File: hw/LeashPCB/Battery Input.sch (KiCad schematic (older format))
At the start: 2 parts, among them J201 1020-1, J202 1020-1

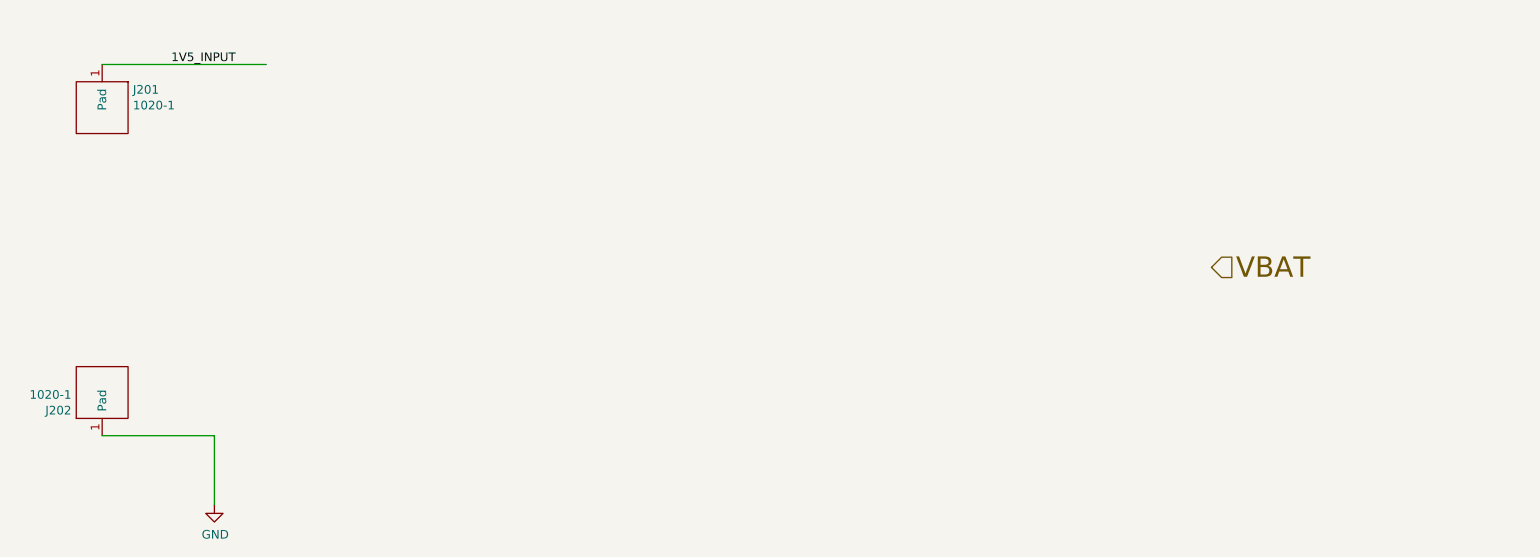
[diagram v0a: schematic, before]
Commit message: Changed some file names to remove spaces and added circuits around the main power chips
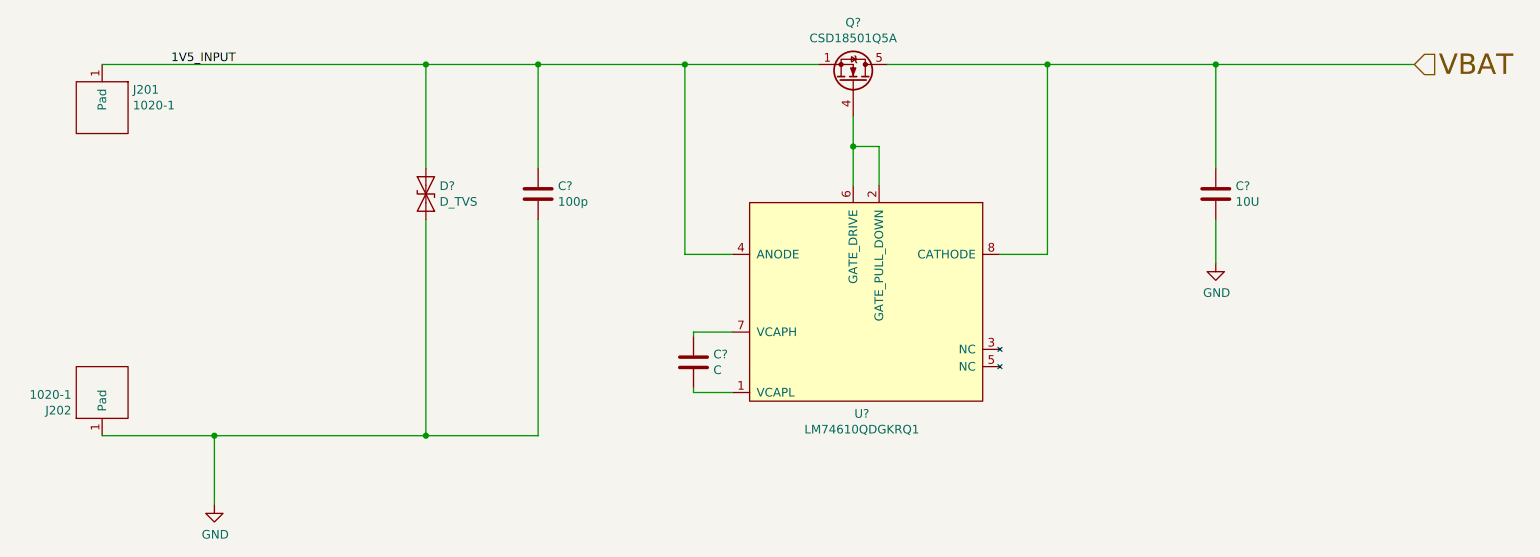
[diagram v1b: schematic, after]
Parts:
- added C?: 100p, symbol Device:C
- added C?: C, symbol Device:C
- added C?: 10U, symbol Device:C
- added D?: D_TVS, symbol Device:D_TVS
- added Q?: CSD18501Q5A, Package_TO_SOT_SMD:TDSON-8-1, symbol Transistor_FET:CSD18501Q5A
- added U?: LM74610QDGKRQ1, symbol LeashPCB:LM74610QDGKRQ1
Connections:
- wire segments 3 -> 29
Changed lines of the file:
@@
 	0    1    1    0
 $EndComp
-Wire Wire Line
-	2650 2050 3600 2050
-Text HLabel 9075 3225 2    118  Input ~ 0
+Text HLabel 10250 2050 2    118  Input ~ 0
 VBAT
 Text Label 3050 2050 0    50   ~ 0
 1V5_INPUT
+$Comp
+L Device:D_TVS D?
+U 1 1 5D067AEF
+P 4525 2800
+F 0 "D?" V 4479 2879 50  0000 L CNN
+F 1 "D_TVS" V 4570 2879 50  0000 L CNN
+F 2 "" H 4525 2800 50  0001 C CNN
+F 3 "~" H 4525 2800 50  0001 C CNN
+	1    4525 2800
+	0    1    1    0
+$EndComp
+$Comp
+L Device:C C?
+U 1 1 5D067F64
+P 5175 2800
+F 0 "C?" H 5290 2846 50  0000 L CNN
+F 1 "100p" H 5290 2755 50  0000 L CNN
+F 2 "" H 5213 2650 50  0001 C CNN
+F 3 "~" H 5175 2800 50  0001 C CNN
+	1    5175 2800
+	1    0    0    -1
+$EndComp
+$Comp
+L Device:C C?
+U 1 1 5D0681B7
+P 6075 3775
+F 0 "C?" H 6190 3821 50  0000 L CNN
+F 1 "C" H 6190 3730 50  0000 L CNN
+F 2 "" H 6113 3625 50  0001 C CNN
+F 3 "~" H 6075 3775 50  0001 C CNN
+	1    6075 3775
+	1    0    0    -1
+$EndComp
+$Comp
+L LeashPCB:LM74610QDGKRQ1 U?
+U 1 1 5D069D70
+P 7150 3400
+F 0 "U?" H 7050 2727 50  0000 C CNN
+F 1 "LM74610QDGKRQ1" H 7050 2636 50  0000 C CNN
+F 2 "" H 6400 3100 50  0001 C CNN
+F 3 "" H 6400 3100 50  0001 C CNN
+	1    7150 3400
+	1    0    0    -1
+$EndComp
+Wire Wire Line
+	6075 3625 6075 3600
+Wire Wire Line
+	6075 3600 6300 3600
+Wire Wire Line
+	6075 3925 6075 3950
+Wire Wire Line
+	6075 3950 6300 3950
+$Comp
+L Device:C C?
+U 1 1 5D06EB1F
+P 9100 2800
+F 0 "C?" H 9215 2846 50  0000 L CNN
+F 1 "10U" H 9215 2755 50  0000 L CNN
+F 2 "" H 9138 2650 50  0001 C CNN
+F 3 "~" H 9100 2800 50  0001 C CNN
+	1    9100 2800
+	1    0    0    -1
+$EndComp
+Wire Wire Line
+	4525 2050 4525 2650
+Wire Wire Line
+	2650 2050 4525 2050
+Wire Wire Line
+	4525 2950 4525 4200
+Connection ~ 3300 4200
+Wire Wire Line
+	4525 2050 5175 2050
+Wire Wire Line
+	5175 2050 5175 2650
+Wire Wire Line
+	3300 4200 4525 4200
+Wire Wire Line
+	5175 2950 5175 4200
+Connection ~ 4525 2050
+Connection ~ 4525 4200
+Wire Wire Line
+	4525 4200 5175 4200
+$Comp
+L power:GND #PWR?
+U 1 1 5D071998
+P 9100 3200
+F 0 "#PWR?" H 9100 2950 50  0001 C CNN
+F 1 "GND" H 9105 3027 50  0000 C CNN
+F 2 "" H 9100 3200 50  0001 C CNN
+F 3 "" H 9100 3200 50  0001 C CNN
+	1    9100 3200
+	1    0    0    -1
+$EndComp
+$Comp
+L Transistor_FET:CSD18501Q5A Q?
+U 1 1 5D0747C0
+P 7000 2150
+F 0 "Q?" V 7343 2150 50  0000 C CNN
+F 1 "CSD18501Q5A" V 7252 2150 50  0000 C CNN
+F 2 "Package_TO_SOT_SMD:TDSON-8-1" H 7200 2075 50  0001 L CIN
+F 3 "http://www.ti.com/lit/gpn/csd18501q5a" V 7000 2150 50  0001 L CNN
+	1    7000 2150
+	0    1    -1   0
+$EndComp
+Wire Wire Line
+	6800 2050 6025 2050
+Connection ~ 5175 2050
+Wire Wire Line
+	7000 2350 7000 2525
+Wire Wire Line
+	7000 2525 7150 2525
+Wire Wire Line
+	7150 2525 7150 2750
+Connection ~ 7000 2525
+Wire Wire Line
+	7000 2525 7000 2750
+Wire Wire Line
+	7200 2050 8125 2050
+Wire Wire Line
+	9100 2650 9100 2050
+Connection ~ 9100 2050
+Wire Wire Line
+	9100 2050 10250 2050
+Wire Wire Line
+	9100 2950 9100 3200
+Wire Wire Line
+	7850 3150 8125 3150
+Wire Wire Line
+	8125 3150 8125 2050
+Connection ~ 8125 2050
+Wire Wire Line
+	8125 2050 9100 2050
+Wire Wire Line
+	6300 3150 6025 3150
+Wire Wire Line
+	6025 3150 6025 2050
+Connection ~ 6025 2050
+Wire Wire Line
+	6025 2050 5175 2050
 $EndSCHEMATC
